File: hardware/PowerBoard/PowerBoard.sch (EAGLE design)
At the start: 136 parts, among them J1 CON-HRS-DM3AT, J2 CON-ZX62R-B-5P, J3 CON-FTSH-105-01-L-DV-K, J4 CON-S2B-PH-SM4-TB, J5 CON-PJ-102A, J6 CON-71741-0002-TOP, M1 MOUNT-HOLE3.3, M2 MOUNT-HOLE3.3, M3 MOUNT-HOLE3.3, M4 MOUNT-HOLE3.3, M5 FIDUCIAL1X2, M6 FIDUCIAL1X2, M7 FIDUCIAL1X2, M8 FIDUCIAL1X2, Q1 SI2323CDS, Q2 SI2312CDS, Q3 SI2333CDS, Q4 SI2333CDS, SW1 SWITCH-SPST, SW2 SWITCH-MS12ASG30, SW3 SWITCH-KSC-201J, U1 LTC4361-2DC, U10 MAX9938FEUK, U11 MAX9938FEUK, U12 MAX9938FEUK, U13 STM32F10XCXT6, U14 LTC2942-1, U15 USBLC6-2, U2 LTC4085, U3 XC6220B331MR-G, U4 XC6220B331MR-G, U5 XC9236A15DMR-G, U6 MIC94043, U8 MAX9938FEUK, U9 MAX9938FEUK, X1 ECX-2236, X2 ECX-31B

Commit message: - Layout update
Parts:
- removed R3, R54: 0, powerboard:R0603
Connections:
- net AGND: no longer R3.2, R54.2
- net DGND: no longer R3.1, R54.1
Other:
- moved on the sheet: R55, R56, R57
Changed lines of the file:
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@@
 <part name="PORT24" library="powerboard" deviceset="PORT7" device=""/>
 <part name="PORT27" library="powerboard" deviceset="PORT15" device=""/>
-<part name="R3" library="powerboard" deviceset="R" device="0603" value="0">
-<attribute name="TOLERANCE" value=""/>
-</part>
-<part name="R54" library="powerboard" deviceset="R" device="0603" value="0">
-<attribute name="TOLERANCE" value=""/>
-</part>
 <part name="R55" library="powerboard" deviceset="R" device="0603" value="0">
 <attribute name="TOLERANCE" value=""/>
@@
 <instance part="FRAME3" gate="G$1" x="0" y="0"/>
 <instance part="FRAME3" gate="G$2" x="147.32" y="0"/>
-<instance part="U$19" gate="G$1" x="228.6" y="55.88"/>
+<instance part="U$19" gate="G$1" x="228.6" y="53.34"/>
 <instance part="R45" gate="G$1" x="220.98" y="48.26" rot="R90"/>
-<instance part="U$20" gate="G$1" x="228.6" y="33.02"/>
+<instance part="U$20" gate="G$1" x="228.6" y="35.56"/>
 <instance part="C17" gate="G$1" x="190.5" y="132.08"/>
 <instance part="C18" gate="G$1" x="198.12" y="132.08"/>
@@
 <instance part="PORT81" gate="G$1" x="10.16" y="66.04" rot="R270"/>
 <instance part="U$66" gate="G$1" x="10.16" y="93.98" smashed="yes"/>
-<instance part="R3" gate="G$1" x="213.36" y="48.26" rot="R90"/>
-<instance part="R54" gate="G$1" x="205.74" y="48.26" rot="R90"/>
-<instance part="R55" gate="G$1" x="198.12" y="48.26" rot="R90"/>
-<instance part="R56" gate="G$1" x="190.5" y="48.26" rot="R90"/>
-<instance part="R57" gate="G$1" x="182.88" y="48.26" rot="R90"/>
+<instance part="R55" gate="G$1" x="213.36" y="48.26" rot="R90"/>
+<instance part="R56" gate="G$1" x="205.74" y="48.26" rot="R90"/>
+<instance part="R57" gate="G$1" x="198.12" y="48.26" rot="R90"/>
 <instance part="TP14" gate="G$1" x="43.18" y="20.32" rot="R180"/>
 <instance part="PORT85" gate="G$1" x="43.18" y="35.56" rot="R90"/>
@@
 <net name="AGND" class="0">
 <segment>
-<wire x1="220.98" y1="50.8" x2="220.98" y2="58.42" width="0.1524" layer="91"/>
-<wire x1="220.98" y1="58.42" x2="228.6" y2="58.42" width="0.1524" layer="91"/>
+<wire x1="220.98" y1="50.8" x2="220.98" y2="55.88" width="0.1524" layer="91"/>
+<wire x1="220.98" y1="55.88" x2="228.6" y2="55.88" width="0.1524" layer="91"/>
 <pinref part="R45" gate="G$1" pin="2"/>
 <pinref part="U$19" gate="G$1" pin="AGND"/>
-<wire x1="220.98" y1="58.42" x2="213.36" y2="58.42" width="0.1524" layer="91"/>
 <pinref part="R57" gate="G$1" pin="2"/>
-<wire x1="213.36" y1="58.42" x2="205.74" y2="58.42" width="0.1524" layer="91"/>
-<wire x1="205.74" y1="58.42" x2="198.12" y2="58.42" width="0.1524" layer="91"/>
-<wire x1="198.12" y1="58.42" x2="190.5" y2="58.42" width="0.1524" layer="91"/>
-<wire x1="190.5" y1="58.42" x2="182.88" y2="58.42" width="0.1524" layer="91"/>
-<wire x1="182.88" y1="58.42" x2="182.88" y2="50.8" width="0.1524" layer="91"/>
+<wire x1="220.98" y1="55.88" x2="213.36" y2="55.88" width="0.1524" layer="91"/>
+<wire x1="213.36" y1="55.88" x2="205.74" y2="55.88" width="0.1524" layer="91"/>
+<wire x1="205.74" y1="55.88" x2="198.12" y2="55.88" width="0.1524" layer="91"/>
+<wire x1="198.12" y1="55.88" x2="198.12" y2="50.8" width="0.1524" layer="91"/>
 <pinref part="R56" gate="G$1" pin="2"/>
-<wire x1="190.5" y1="58.42" x2="190.5" y2="50.8" width="0.1524" layer="91"/>
+<wire x1="205.74" y1="55.88" x2="205.74" y2="50.8" width="0.1524" layer="91"/>
 <pinref part="R55" gate="G$1" pin="2"/>
-<wire x1="198.12" y1="58.42" x2="198.12" y2="50.8" width="0.1524" layer="91"/>
-<pinref part="R54" gate="G$1" pin="2"/>
-<wire x1="205.74" y1="58.42" x2="205.74" y2="50.8" width="0.1524" layer="91"/>
-<pinref part="R3" gate="G$1" pin="2"/>
-<wire x1="213.36" y1="58.42" x2="213.36" y2="50.8" width="0.1524" layer="91"/>
-<junction x="190.5" y="58.42"/>
-<junction x="198.12" y="58.42"/>
-<junction x="205.74" y="58.42"/>
-<junction x="213.36" y="58.42"/>
-<junction x="220.98" y="58.42"/>
+<wire x1="213.36" y1="55.88" x2="213.36" y2="50.8" width="0.1524" layer="91"/>
+<junction x="205.74" y="55.88"/>
+<junction x="213.36" y="55.88"/>
+<junction x="220.98" y="55.88"/>
 </segment>
 <segment>
@@
 <net name="DGND" class="0">
 <segment>
-<wire x1="228.6" y1="35.56" x2="220.98" y2="35.56" width="0.1524" layer="91"/>
-<wire x1="220.98" y1="35.56" x2="220.98" y2="43.18" width="0.1524" layer="91"/>
+<wire x1="228.6" y1="38.1" x2="220.98" y2="38.1" width="0.1524" layer="91"/>
+<wire x1="220.98" y1="38.1" x2="220.98" y2="43.18" width="0.1524" layer="91"/>
 <pinref part="U$20" gate="G$1" pin="DGND"/>
 <pinref part="R45" gate="G$1" pin="1"/>
 <pinref part="R57" gate="G$1" pin="1"/>
-<wire x1="182.88" y1="43.18" x2="182.88" y2="35.56" width="0.1524" layer="91"/>
-<wire x1="182.88" y1="35.56" x2="190.5" y2="35.56" width="0.1524" layer="91"/>
+<wire x1="198.12" y1="43.18" x2="198.12" y2="38.1" width="0.1524" layer="91"/>
+<wire x1="198.12" y1="38.1" x2="205.74" y2="38.1" width="0.1524" layer="91"/>
 <pinref part="R56" gate="G$1" pin="1"/>
-<wire x1="190.5" y1="35.56" x2="198.12" y2="35.56" width="0.1524" layer="91"/>
-<wire x1="198.12" y1="35.56" x2="205.74" y2="35.56" width="0.1524" layer="91"/>
-<wire x1="205.74" y1="35.56" x2="213.36" y2="35.56" width="0.1524" layer="91"/>
-<wire x1="213.36" y1="35.56" x2="220.98" y2="35.56" width="0.1524" layer="91"/>
-<wire x1="190.5" y1="43.18" x2="190.5" y2="35.56" width="0.1524" layer="91"/>
+<wire x1="205.74" y1="38.1" x2="213.36" y2="38.1" width="0.1524" layer="91"/>
+<wire x1="213.36" y1="38.1" x2="220.98" y2="38.1" width="0.1524" layer="91"/>
+<wire x1="205.74" y1="43.18" x2="205.74" y2="38.1" width="0.1524" layer="91"/>
 <pinref part="R55" gate="G$1" pin="1"/>
-<wire x1="198.12" y1="43.18" x2="198.12" y2="35.56" width="0.1524" layer="91"/>
-<pinref part="R54" gate="G$1" pin="1"/>
-<wire x1="205.74" y1="43.18" x2="205.74" y2="35.56" width="0.1524" layer="91"/>
-<pinref part="R3" gate="G$1" pin="1"/>
-<wire x1="213.36" y1="43.18" x2="213.36" y2="35.56" width="0.1524" layer="91"/>
-<junction x="220.98" y="35.56"/>
-<junction x="213.36" y="35.56"/>
-<junction x="205.74" y="35.56"/>
-<junction x="198.12" y="35.56"/>
-<junction x="190.5" y="35.56"/>
-</segment>
-<segment>
+<wire x1="213.36" y1="43.18" x2="213.36" y2="38.1" width="0.1524" layer="91"/>
+<junction x="220.98" y="38.1"/>
+<junction x="213.36" y="38.1"/>
+<junction x="205.74" y="38.1"/>
+</segment>
+<segment>

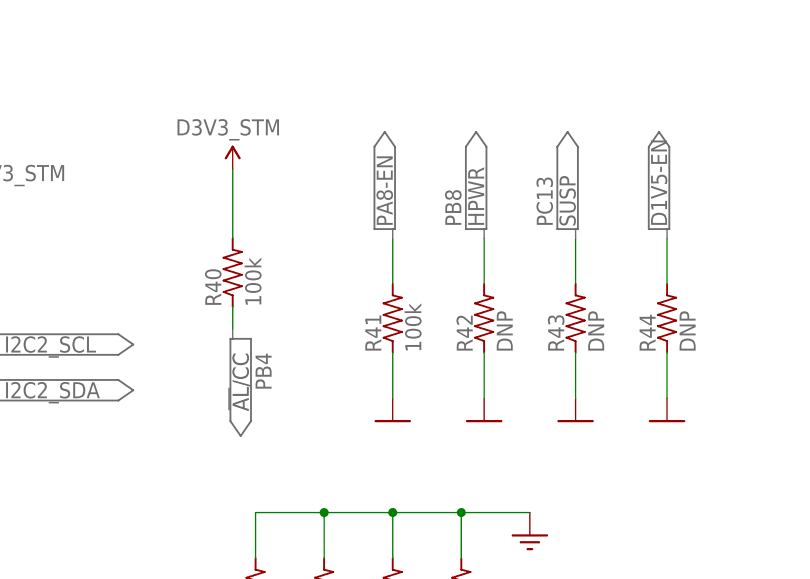
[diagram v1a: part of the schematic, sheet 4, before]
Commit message: - Layout update - PB4, PC13 pins changed
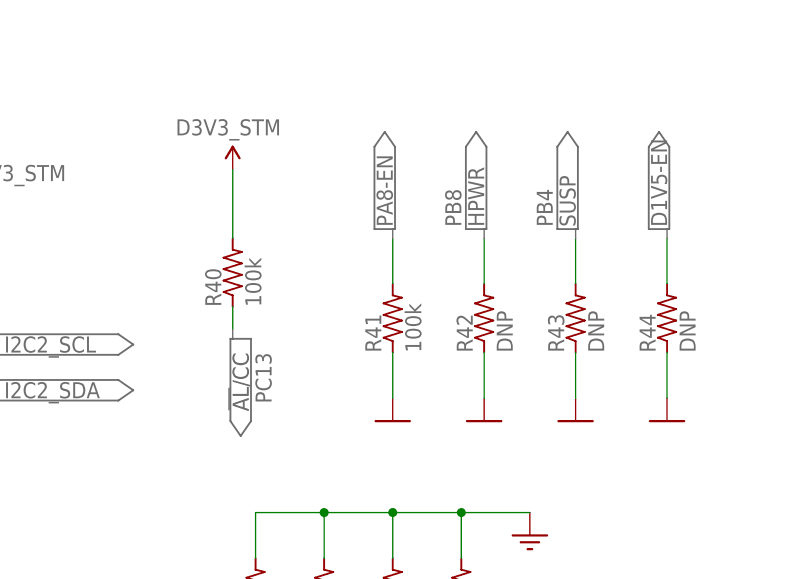
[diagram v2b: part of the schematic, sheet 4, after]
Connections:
- net PB4: now also R43.2, U2.SUSP; no longer R40.1, U14.!AL!/CC
- net PC13: now also R40.1, U14.!AL!/CC; no longer R43.2, U2.SUSP
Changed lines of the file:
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@@
-</segment>
-</net>
-<net name="PC13" class="0">
-<segment>
-<wire x1="149.86" y1="129.54" x2="147.32" y2="129.54" width="0.1524" layer="91"/>
-<label x="144.78" y="129.54" size="1.778" layer="95" rot="MR0"/>
-<pinref part="U2" gate="G$1" pin="SUSP"/>
 </segment>
 </net>
@@
 <label x="134.62" y="20.32" size="1.778" layer="95"/>
 <pinref part="U6" gate="G$1" pin="VOUT"/>
+</segment>
+</net>
+<net name="PB4" class="0">
+<segment>
+<wire x1="149.86" y1="129.54" x2="147.32" y2="129.54" width="0.1524" layer="91"/>
+<label x="144.78" y="129.54" size="1.778" layer="95" rot="MR0"/>
+<pinref part="U2" gate="G$1" pin="SUSP"/>
 </segment>
 </net>
@@
 <pinref part="U13" gate="-PORTB_L" pin="PB4"/>
 </segment>
-<segment>
-<wire x1="109.22" y1="17.78" x2="106.68" y2="17.78" width="0.1524" layer="91"/>
-<label x="104.14" y="17.78" size="1.778" layer="95" rot="MR0"/>
-<pinref part="U14" gate="LTC3677-2" pin="!AL!/CC"/>
-</segment>
 </net>
 <net name="PB2" class="0">
@@
 <label x="182.88" y="73.66" size="1.778" layer="95"/>
 <pinref part="U13" gate="-PORTC" pin="PC13"/>
+</segment>
+<segment>
+<wire x1="109.22" y1="17.78" x2="106.68" y2="17.78" width="0.1524" layer="91"/>
+<label x="104.14" y="17.78" size="1.778" layer="95" rot="MR0"/>
+<pinref part="U14" gate="LTC3677-2" pin="!AL!/CC"/>
 </segment>
 </net>
@@
 </segment>
 </net>
-<net name="PC13" class="0">
+<net name="D1V5-EN" class="0">
+<segment>
+<wire x1="243.84" y1="81.28" x2="243.84" y2="86.36" width="0.1524" layer="91"/>
+<label x="243.84" y="87.63" size="1.778" layer="95" rot="R90"/>
+<pinref part="R44" gate="G$1" pin="2"/>
+</segment>
+</net>
+<net name="USBDP" class="0">
+<segment>
+<wire x1="10.16" y1="78.74" x2="10.16" y2="76.2" width="0.1524" layer="91"/>
+<label x="10.16" y="73.66" size="1.778" layer="95" rot="R270"/>
+<pinref part="R53" gate="G$1" pin="1"/>
+</segment>
+</net>
+<net name="VSUP_I" class="0">
+<segment>
+<wire x1="71.12" y1="134.62" x2="71.12" y2="137.16" width="0.1524" layer="91"/>
+<label x="71.12" y="139.7" size="1.778" layer="95" rot="R90"/>
+<pinref part="C9" gate="G$1" pin="1"/>
+</segment>
+<segment>
+<wire x1="99.06" y1="134.62" x2="99.06" y2="137.16" width="0.1524" layer="91"/>
+<label x="99.06" y="139.7" size="1.778" layer="95" rot="R90"/>
+<pinref part="C11" gate="G$1" pin="1"/>
+</segment>
+<segment>
+<wire x1="127" y1="134.62" x2="127" y2="137.16" width="0.1524" layer="91"/>
+<label x="127" y="139.7" size="1.778" layer="95" rot="R90"/>
+<pinref part="C13" gate="G$1" pin="1"/>
+</segment>
+</net>
+<net name="PB4" class="0">
 <segment>
 <wire x1="233.68" y1="81.28" x2="233.68" y2="86.36" width="0.1524" layer="91"/>
@@
 </segment>
 </net>
-<net name="D1V5-EN" class="0">
-<segment>
-<wire x1="243.84" y1="81.28" x2="243.84" y2="86.36" width="0.1524" layer="91"/>
-<label x="243.84" y="87.63" size="1.778" layer="95" rot="R90"/>
-<pinref part="R44" gate="G$1" pin="2"/>
-</segment>
-</net>
-<net name="USBDP" class="0">
-<segment>
-<wire x1="10.16" y1="78.74" x2="10.16" y2="76.2" width="0.1524" layer="91"/>
-<label x="10.16" y="73.66" size="1.778" layer="95" rot="R270"/>
-<pinref part="R53" gate="G$1" pin="1"/>
-</segment>
-</net>
-<net name="VSUP_I" class="0">
-<segment>
-<wire x1="71.12" y1="134.62" x2="71.12" y2="137.16" width="0.1524" layer="91"/>
-<label x="71.12" y="139.7" size="1.778" layer="95" rot="R90"/>
-<pinref part="C9" gate="G$1" pin="1"/>
-</segment>
-<segment>
-<wire x1="99.06" y1="134.62" x2="99.06" y2="137.16" width="0.1524" layer="91"/>
-<label x="99.06" y="139.7" size="1.778" layer="95" rot="R90"/>
-<pinref part="C11" gate="G$1" pin="1"/>
-</segment>
-<segment>
-<wire x1="127" y1="134.62" x2="127" y2="137.16" width="0.1524" layer="91"/>
-<label x="127" y="139.7" size="1.778" layer="95" rot="R90"/>
-<pinref part="C13" gate="G$1" pin="1"/>
-</segment>
-</net>
-<net name="PB4" class="0">
+<net name="PC13" class="0">
 <segment>
 <wire x1="195.58" y1="78.74" x2="195.58" y2="76.2" width="0.1524" layer="91"/>

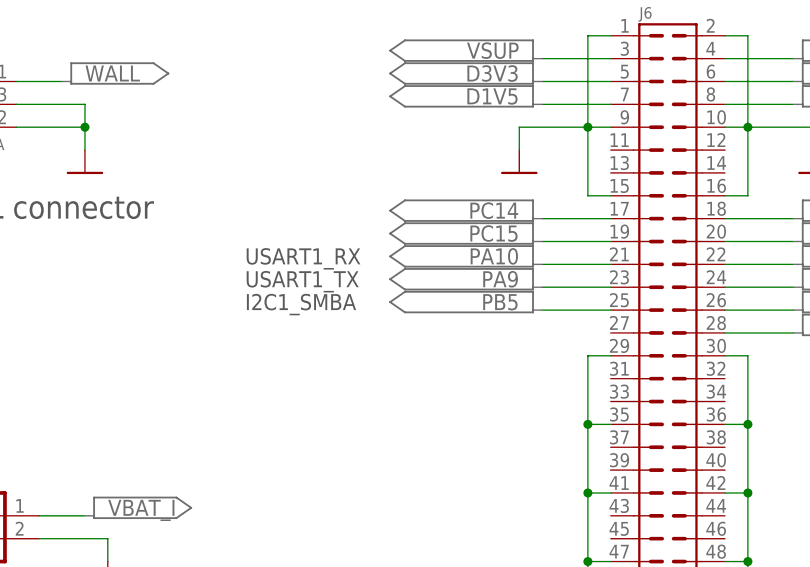
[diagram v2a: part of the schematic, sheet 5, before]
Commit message: - Layout update - AGND and DGND vias - PC15 selectable to connect either to Wake up or GPIO interface pin
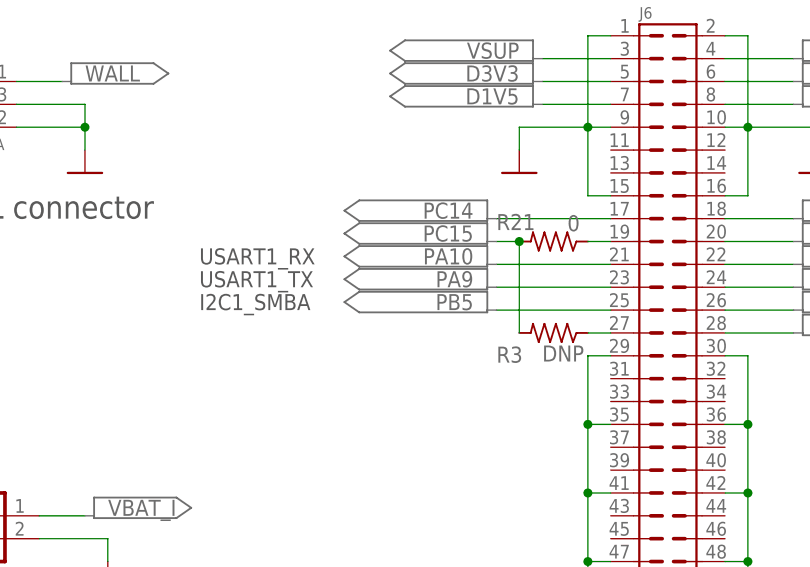
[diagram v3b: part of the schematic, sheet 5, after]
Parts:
- added R21: 0, powerboard:R0603
- added R3: DNP, powerboard:R0603
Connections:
- new net N$7: J6.27, R3.1
- new net N$9: J6.19, R21.1
- net PB4: now also R40.1, U14.!AL!/CC; no longer R43.2, U2.SUSP
- net PC13: now also R43.2, U2.SUSP; no longer R40.1, U14.!AL!/CC
- net PC15: now also R21.2, R3.2; no longer J6.19
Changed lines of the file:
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@@
 <part name="U$70" library="powerboard" deviceset="DGND" device=""/>
 <part name="PORT65" library="powerboard" deviceset="PORT7" device=""/>
+<part name="R3" library="powerboard" deviceset="R" device="0603" value="DNP">
+<attribute name="TOLERANCE" value=""/>
+</part>
+<part name="R21" library="powerboard" deviceset="R" device="0603" value="0">
+<attribute name="TOLERANCE" value=""/>
+</part>
 </parts>
 <sheets>
@@
 </segment>
 </net>
-<net name="PB4" class="0">
+<net name="PC13" class="0">
 <segment>
 <wire x1="149.86" y1="129.54" x2="147.32" y2="129.54" width="0.1524" layer="91"/>
@@
 <pinref part="U13" gate="-PORTB_L" pin="PB4"/>
 </segment>
+<segment>
+<wire x1="109.22" y1="17.78" x2="106.68" y2="17.78" width="0.1524" layer="91"/>
+<label x="104.14" y="17.78" size="1.778" layer="95" rot="MR0"/>
+<pinref part="U14" gate="LTC3677-2" pin="!AL!/CC"/>
+</segment>
 </net>
 <net name="PB2" class="0">
@@
 <label x="182.88" y="73.66" size="1.778" layer="95"/>
 <pinref part="U13" gate="-PORTC" pin="PC13"/>
-</segment>
-<segment>
-<wire x1="109.22" y1="17.78" x2="106.68" y2="17.78" width="0.1524" layer="91"/>
-<label x="104.14" y="17.78" size="1.778" layer="95" rot="MR0"/>
-<pinref part="U14" gate="LTC3677-2" pin="!AL!/CC"/>
 </segment>
 </net>
@@
 <net name="PB4" class="0">
 <segment>
+<wire x1="195.58" y1="78.74" x2="195.58" y2="76.2" width="0.1524" layer="91"/>
+<label x="198.12" y="73.66" size="1.778" layer="95" rot="R270"/>
+<pinref part="R40" gate="G$1" pin="1"/>
+</segment>
+</net>
+<net name="PC13" class="0">
+<segment>
 <wire x1="233.68" y1="81.28" x2="233.68" y2="86.36" width="0.1524" layer="91"/>
 <label x="231.14" y="87.63" size="1.778" layer="95" rot="R90"/>
 <pinref part="R43" gate="G$1" pin="2"/>
-</segment>
-</net>
-<net name="PC13" class="0">
-<segment>
-<wire x1="195.58" y1="78.74" x2="195.58" y2="76.2" width="0.1524" layer="91"/>
-<label x="198.12" y="73.66" size="1.778" layer="95" rot="R270"/>
-<pinref part="R40" gate="G$1" pin="1"/>
 </segment>
 </net>
@@
 <text x="111.76" y="86.36" size="2.54" layer="97">Battery connector</text>
 <text x="115.57" y="46.99" size="2.54" layer="97">Slide switch</text>
-<text x="147.32" y="124.46" size="1.778" layer="97">USART1_TX</text>
-<text x="147.32" y="127" size="1.778" layer="97">USART1_RX</text>
-<text x="147.32" y="121.92" size="1.778" layer="97">I2C1_SMBA</text>
+<text x="142.24" y="124.46" size="1.778" layer="97">USART1_TX</text>
+<text x="142.24" y="127" size="1.778" layer="97">USART1_RX</text>
+<text x="142.24" y="121.92" size="1.778" layer="97">I2C1_SMBA</text>
 </plain>
 <instances>
@@
 <instance part="PORT96" gate="G$1" x="223.52" y="127"/>
 <instance part="PORT97" gate="G$1" x="223.52" y="129.54"/>
-<instance part="PORT98" gate="G$1" x="165.1" y="132.08" rot="MR0"/>
-<instance part="PORT99" gate="G$1" x="165.1" y="129.54" rot="MR0"/>
-<instance part="PORT100" gate="G$1" x="165.1" y="124.46" rot="MR0"/>
+<instance part="PORT98" gate="G$1" x="160.02" y="132.08" rot="MR0"/>
+<instance part="PORT99" gate="G$1" x="160.02" y="129.54" rot="MR0"/>
+<instance part="PORT100" gate="G$1" x="160.02" y="124.46" rot="MR0"/>
 <instance part="PORT115" gate="G$1" x="165.1" y="144.78" rot="MR0"/>
 <instance part="PORT117" gate="G$1" x="223.52" y="144.78"/>
@@
 <instance part="PORT119" gate="G$1" x="223.52" y="53.34"/>
 <instance part="PORT120" gate="G$1" x="223.52" y="50.8"/>
-<instance part="PORT89" gate="G$1" x="165.1" y="127" rot="MR0"/>
+<instance part="PORT89" gate="G$1" x="160.02" y="127" rot="MR0"/>
 <instance part="U$4" gate="G$1" x="177.8" y="137.16"/>
 <instance part="U15" gate="G$1" x="53.34" y="99.06"/>
@@
 <instance part="PORT2" gate="G$1" x="223.52" y="121.92"/>
 <instance part="PORT24" gate="G$1" x="223.52" y="119.38"/>
-<instance part="PORT92" gate="G$1" x="165.1" y="121.92" rot="MR0"/>
+<instance part="PORT92" gate="G$1" x="160.02" y="121.92" rot="MR0"/>
+<instance part="R3" gate="G$1" x="180.34" y="119.38" smashed="yes" rot="R180">
+<attribute name="NAME" x="175.26" y="116.078" size="1.778" layer="95"/>
+<attribute name="VALUE" x="180.34" y="116.205" size="1.778" layer="96"/>
+</instance>
+<instance part="R21" gate="G$1" x="180.34" y="129.54" smashed="yes" rot="R180">
+<attribute name="NAME" x="175.26" y="130.81" size="1.778" layer="95"/>
+<attribute name="VALUE" x="183.134" y="130.683" size="1.778" layer="96"/>
+</instance>
 </instances>
 <busses>
@@
 <label x="210.82" y="53.34" size="1.778" layer="95"/>
 <pinref part="J6" gate="G$1" pin="80"/>
-</segment>
-</net>
-<net name="PC14" class="0">
-<segment>
-<wire x1="180.34" y1="132.08" x2="187.96" y2="132.08" width="0.1524" layer="91"/>
-<label x="177.8" y="132.08" size="1.778" layer="95" rot="MR0"/>
-<pinref part="J6" gate="G$1" pin="17"/>
-</segment>
-</net>
-<net name="PC15" class="0">
-<segment>
-<wire x1="180.34" y1="129.54" x2="187.96" y2="129.54" width="0.1524" layer="91"/>
-<label x="177.8" y="129.54" size="1.778" layer="95" rot="MR0"/>
-<pinref part="J6" gate="G$1" pin="19"/>
 </segment>
 </net>
@@
 <net name="PA10" class="0">
 <segment>
-<label x="177.8" y="127" size="1.778" layer="95" rot="MR0"/>
+<label x="172.72" y="127" size="1.778" layer="95" rot="MR0"/>
 <pinref part="J6" gate="G$1" pin="21"/>
-<wire x1="180.34" y1="127" x2="187.96" y2="127" width="0.1524" layer="91"/>
+<wire x1="175.26" y1="127" x2="187.96" y2="127" width="0.1524" layer="91"/>
 </segment>
 </net>
 <net name="PA9" class="0">
 <segment>
-<label x="177.8" y="124.46" size="1.778" layer="95" rot="MR0"/>
+<label x="172.72" y="124.46" size="1.778" layer="95" rot="MR0"/>
 <pinref part="J6" gate="G$1" pin="23"/>
-<wire x1="180.34" y1="124.46" x2="187.96" y2="124.46" width="0.1524" layer="91"/>
+<wire x1="175.26" y1="124.46" x2="187.96" y2="124.46" width="0.1524" layer="91"/>
 </segment>
 </net>
@@
 <net name="PB5" class="0">
 <segment>
-<label x="177.8" y="121.92" size="1.778" layer="95" rot="MR0"/>
+<label x="172.72" y="121.92" size="1.778" layer="95" rot="MR0"/>
 <pinref part="J6" gate="G$1" pin="25"/>
-<wire x1="180.34" y1="121.92" x2="187.96" y2="121.92" width="0.1524" layer="91"/>
-</segment>
-</net>
+<wire x1="175.26" y1="121.92" x2="187.96" y2="121.92" width="0.1524" layer="91"/>
+</segment>
+</net>
+<net name="N$7" class="0">
+<segment>
+<pinref part="J6" gate="G$1" pin="27"/>
+<pinref part="R3" gate="G$1" pin="1"/>
+<wire x1="187.96" y1="119.38" x2="185.42" y2="119.38" width="0.1524" layer="91"/>
+</segment>
+</net>
+<net name="PC14" class="0">
+<segment>
+<pinref part="J6" gate="G$1" pin="17"/>
+<wire x1="187.96" y1="132.08" x2="175.26" y2="132.08" width="0.1524" layer="91"/>
+<label x="172.72" y="132.08" size="1.778" layer="95" rot="MR0"/>
+</segment>
+</net>
+<net name="N$9" class="0">
+<segment>
+<pinref part="J6" gate="G$1" pin="19"/>
+<pinref part="R21" gate="G$1" pin="1"/>
+<wire x1="187.96" y1="129.54" x2="185.42" y2="129.54" width="0.1524" layer="91"/>
+</segment>
+</net>
+<net name="PC15" class="0">
+<segment>
+<pinref part="R21" gate="G$1" pin="2"/>
+<wire x1="177.8" y1="129.54" x2="175.26" y2="129.54" width="0.1524" layer="91"/>
+<label x="172.72" y="129.54" size="1.778" layer="95" rot="MR0"/>
+<pinref part="R3" gate="G$1" pin="2"/>
+<wire x1="177.8" y1="119.38" x2="177.8" y2="129.54" width="0.1524" layer="91"/>
+<junction x="177.8" y="129.54"/>
+</segment>
+</net>
